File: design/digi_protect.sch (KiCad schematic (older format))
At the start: 2 parts

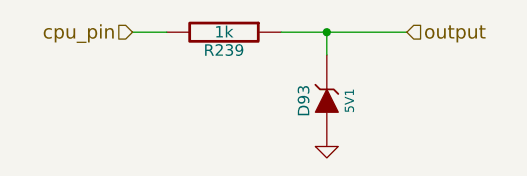
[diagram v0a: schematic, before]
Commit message: updating bom, lets commit this before I run a script to update the footprints for the resistors
Signed-off-by: Jared Harvey <TortiseGIT@jaredharvey.com>
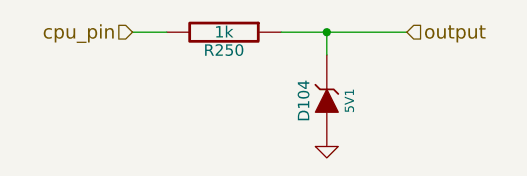
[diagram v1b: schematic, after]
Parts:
- D99: footprint (none) -> SOD-123
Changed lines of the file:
@@
-EESchema Schematic File Version 2  date 2/14/2011 7:45:17 AM
+EESchema Schematic File Version 2  date 2/16/2011 5:39:14 AM
 LIBS:power
 LIBS:freeEMS_lib
@@
 EELAYER END
 $Descr A4 11700 8267
-Sheet 13 55
+Sheet 13 56
 Title "Puma board"
-Date "14 feb 2011"
+Date "16 feb 2011"
 Rev "v0.02"
 Comp "diyefi.org"
@@
 AR Path="/4CD743EC/4CD742CA" Ref="#PWR020"  Part="1"
 AR Path="/4CD743DA/4CD742CA" Ref="#PWR021"  Part="1"
-F 0 "#PWR022" H 4600 3450 30  0001 C CNN
+F 0 "#PWR011" H 4600 3450 30  0001 C CNN
 F 1 "GND" H 4600 3380 30  0001 C CNN
 	1    4600 3450
@@
 AR Path="/4CD743EC/4CD742B5" Ref="D95"  Part="1"
 AR Path="/4CD743DA/4CD742B5" Ref="D94"  Part="1"
-F 0 "D93" H 4600 3350 50  0000 C CNN
+F 0 "D104" H 4600 3350 50  0000 C CNN
 F 1 "5V1" H 4600 3150 40  0000 C CNN
+F 2 "SOD-123" H 4600 3250 60  0001 C CNN
 F 4 "Diodes Inc" V 1130 2600 60  0001 C CNN "mfg"
 F 5 "BZT52C5V1-7-F" V 1130 2600 60  0001 C CNN "mfg#"
@@
 AR Path="/4CD743EC/4CD742AE" Ref="R241"  Part="1"
 AR Path="/4CD743DA/4CD742AE" Ref="R240"  Part="1"
-F 0 "R239" V 4230 2950 50  0000 C CNN
+F 0 "R250" V 4230 2950 50  0000 C CNN
 F 1 "1k" V 4150 2950 50  0000 C CNN
 F 4 "Stackpole" V 1130 2600 60  0001 C CNN "mfg"

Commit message: Schematic BOM is now fully populated with only 3 exceptions, .cmp file is obsolete at this point, so it has been removed.
Signed-off-by: Jared Harvey <TortiseGIT@jaredharvey.com>
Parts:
- R245: footprint (none) -> SM0805
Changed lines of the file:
@@
-EESchema Schematic File Version 2  date 2/16/2011 5:39:14 AM
+EESchema Schematic File Version 2  date 2/16/2011 8:44:19 AM
 LIBS:power
 LIBS:freeEMS_lib
@@
 AR Path="/4CD743EC/4CD742CA" Ref="#PWR020"  Part="1"
 AR Path="/4CD743DA/4CD742CA" Ref="#PWR021"  Part="1"
-F 0 "#PWR011" H 4600 3450 30  0001 C CNN
+F 0 "#PWR022" H 4600 3450 30  0001 C CNN
 F 1 "GND" H 4600 3380 30  0001 C CNN
 	1    4600 3450
@@
 F 0 "R250" V 4230 2950 50  0000 C CNN
 F 1 "1k" V 4150 2950 50  0000 C CNN
+F 2 "SM0805" V 1130 2600 60  0001 C CNN
 F 4 "Stackpole" V 1130 2600 60  0001 C CNN "mfg"
 F 5 "RMCF0805JT1K00" V 1130 2600 60  0001 C CNN "mfg#"
